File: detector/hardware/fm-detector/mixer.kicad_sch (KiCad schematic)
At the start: 11 parts, among them J3 U.FL, Q3 BSS138

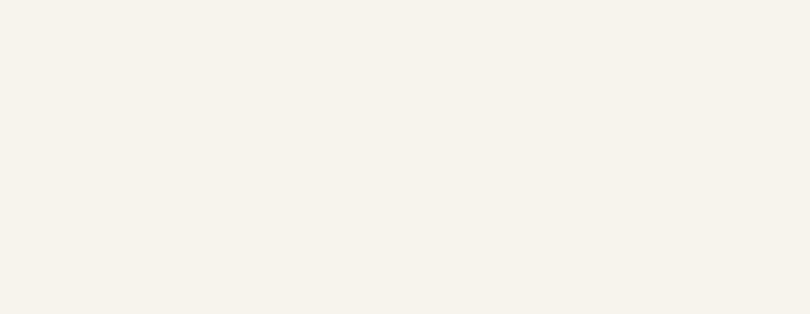
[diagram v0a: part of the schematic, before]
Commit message: Schematic for PCB-0010-0100
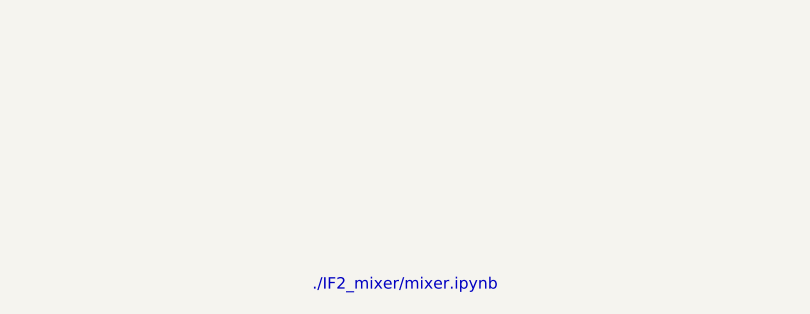
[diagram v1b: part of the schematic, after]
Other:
- note added: "./IF2_mixer/mixer.ipynb"
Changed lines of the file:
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@@
 		(title "IF2 Mixer")
+	)
+	(text "./IF2_mixer/mixer.ipynb"
+		(exclude_from_sim no)
+		(at 114.3 129.54 0)
+		(effects
+			(font
+				(size 1.27 1.27)
+			)
+			(href "https://github.com/LieBtrau/MegawattKS_Radio_Design_101/blob/main/IF2_mixer/mixer.ipynb")
+		)
 	)
 	(junction
